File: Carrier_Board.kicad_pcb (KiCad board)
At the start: 4 copper layers, 185.3 x 105.1 mm, 266 parts, among them J18 USB_C_Receptacle_USB2.0_16P, J4 USB3_A_Stacked, J78 Conn_01x03_Pin, J80 Barrel_Jack_Switch, J81 Conn_01x04_Pin, J82 Conn_01x03_Pin, J83 Conn_01x04_Pin, J84 Conn_01x03_Pin, J85 Conn_01x03_Pin, J86 Conn_01x04_Pin, J87 Conn_01x04_Pin, J88 Conn_01x03_Pin, J89 Bus_PCI_Express_x4, J90 RJ45_RB1-125B8G1A, J91 USB3_A_Stacked, J92 USB_A_Stacked, J93 HDMI_A, J94 Bus_M.2_Socket_M, J95 Bus_M.2_Socket_E, M1 Fan_4pin, M2 Fan_4pin, Q78 2N7002, Q79 2N7002, Q80 AON7262E, Q81 2N7002, Q82 2N7002, Q83 2SK3018, Q84 2SK3018, Q85 2SK3018, SW78 SW_Push, SW79 SW_Push, U14 CH224K, U79 TL431DBZ, U80 LM2734X, U81 LM2734X, U82 D3V3XA4B10LP, U83 D3V3XA4B10LP, U84 D3V3XA4B10LP, U85 D3V3XA4B10LP, U86 RTL8111H-CG-RH, U87 D3V3XA4B10LP, U88 D3V3XA4B10LP, U89 D3V3XA4B10LP, U90 D3V3XA4B10LP, U91 D3V3XA4B10LP, U92 D3V3XA4B10LP, U93 D3V3XA4B10LP, Y78 25MHz

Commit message: Started on physical placement of components but footprint got H6 is incoorect. Schematic needs annotation before importing the changes.
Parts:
- moved BT78 420.7 mm to (51.6, 125.4), turned to 90 degrees
- moved H81 414.5 mm to (44.9, 155.2)
- moved H80 399.6 mm to (44.6, 54.4)
- moved J90 336.7 mm to (61.0, 68.5), turned to -90 degrees
- moved H5 305.9 mm to (167.2, 53.7)
- moved J18 288.9 mm to (225.3, 83.0), turned to 90 degrees
- moved H79 252.8 mm to (226.0, 154.9)
- moved SW78 247.4 mm to (171.8, 155.5)
- moved J95 241.9 mm to (93.9, 92.3), turned to -90 degrees
- moved SW79 234.0 mm to (183.6, 155.5)
- moved A78 224.7 mm to (135.3, 110.6), turned to 180 degrees
- moved H78 221.0 mm to (225.7, 54.7)
- moved J93 219.2 mm to (151.8, 150.8), turned to -90 degrees
- moved J4 203.2 mm to (334.4, 158.2)
- moved J91 202.6 mm to (105.4, 147.3)
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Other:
- board size 185.3 x 105.1 mm -> 190 x 110 mm

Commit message: Updating the pcb and recovering placement of components that were reset
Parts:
- removed C100, C109, C110, C113, C115, C130, C148, C99: 100nF/50V, A_HDJ_Library:C_0402_1005Metric
- removed C101, C102, C103, C104, C105, C106, C107, C108: 220nF/50v, A_HDJ_Library:C_0402_1005Metric
- removed C111, C112: 100uF/100v, A_HDJ_Library:CP_Elec_6.3x7.7
- removed C114: 10uF/10V, A_HDJ_Library:C_0402_1005Metric
- removed C116: 560uF/25V, A_HDJ_Library:CP_Elec_6.3x7.7
- removed C117, C118, C119, C120, C121, C122, C128, C152, C154: 100nF/50v, A_HDJ_Library:C_0402_1005Metric
- removed C127, C129, C151, C153: 10uF/50v, A_HDJ_Library:C_0402_1005Metric
- removed C132: 12pF/50V, A_HDJ_Library:C_0402_1005Metric
- removed C133, C134, C135, C136, C140, C141, C142, C143, C144, C145, C146, C147: 100NF/50V, A_HDJ_Library:C_0402_1005Metric
- removed C137, C138, C139: 22mF/10V, A_HDJ_Library:C_0603_1608Metric
- removed C149, C150: 220nF/50V, A_HDJ_Library:C_0402_1005Metric
- removed C155, C156: 220NF/50V, A_HDJ_Library:C_0402_1005Metric
- removed C157, C159: 10uF/10v, A_HDJ_Library:C_0402_1005Metric
- removed C158, C160: 100uF/10v, A_HDJ_Library:C_0402_1005Metric
- removed C86: 1uF/16V, A_HDJ_Library:C_0402_1005Metric
- removed C87, C88: 100uF/50V, A_HDJ_Library:C_0603_1608Metric
- removed C89, C90, C91, C92, C93, C94, C95, C96, C97, C98: 22uF/10V, A_HDJ_Library:C_0603_1608Metric
- removed D100, D101, D102: ESD5V0B03, A_HDJ_Library:D_0402_1005Metric
- removed D103, D94, D95: 1N5819WS, A_HDJ_Library:D_SOD-323
- removed D104: LED, digikey-footprints:LED_0603
- removed D78, D79, D89, D93, D96, D97, D98, D99: ESD9B5.0ST5G, A_HDJ_Library:D_0402_1005Metric
- removed D80, D81, D82: D_Zener, A_HDJ_Library:D_0402_1005Metric
- removed D83, D84, D85, D86, D87, D88: D_Schottky, A_HDJ_Library:D_SMA
- removed D90, D91: LED, A_HDJ_Library:LED_0603_1608Metric
- removed D92: +3V3 Izt=5mA, Diode_SMD:D_SOD-323
- removed F78, F79, F80, F81: 6V/1A, A_HDJ_Library:Fuse_0805_2012Metric
- removed F82: 6V/50MA, A_HDJ_Library:C_0603_1608Metric
- removed H82, H83: MountingHole_M2.0, A_HDJ_Library:MountingHole_3.2mm_M3_Pad_Via
- removed J80: Barrel_Jack_Switch, A_HDJ_Library:DC_Jack_DC007B_30V_10A
- removed J81, J83, J86, J87: Conn_01x04_Pin, A_HDJ_Library:PinHeader_1x04_P2.54mm_Vertical
- removed J82, J84, J85, J88: Conn_01x03_Pin, A_HDJ_Library:PinHeader_1x03_P2.54mm_Vertical
- removed J89: Bus_PCI_Express_x4, A_HDJ_Library:PCIe_x4_Gen3Slot_Connectors
- removed J90: RJ45_RB1-125B8G1A, A_HDJ_Library:RJ45_UDE_RB1-125B8G1A
- removed JP78: Jumper_3_Bridged12, A_HDJ_Library:PinHeader_1x03_P2.54mm_Vertical
- removed JP79: SolderJumper_2_Open, Jumper:SolderJumper-2_P1.3mm_Bridged_RoundedPad1.0x1.5mm
- removed L78, L79: 2.2UH/4.3A, A_HDJ_Library:L_Sunlord_SWPA4020S
- removed Q78, Q81, Q82: 2N7002, A_HDJ_Library:SOT-23
- removed Q79: 2N7002, Package_TO_SOT_SMD:SOT-23
- removed Q80: AON7262E, A_HDJ_Library:MOSFET_PDFN8_3.3x3.3
- removed Q83, Q84: 2SK3018, A_HDJ_Library:SOT-23
- removed R100, R86, R91, R93: 100K/1%, A_HDJ_Library:R_0402_1005Metric
- removed R101, R99: 2.2k/1%, A_HDJ_Library:R_0402_1005Metric
- removed R102, R98: 100k/1%, A_HDJ_Library:R_0402_1005Metric
- removed R103, R94: 100R/1%, A_HDJ_Library:R_0402_1005Metric
- removed R104, R108, R109, R84, R95, R97: 10k/1%, A_HDJ_Library:R_0402_1005Metric
- removed R105, R112, R113, R114, R116: 21.5k/1%, A_HDJ_Library:R_0402_1005Metric
- removed R106, R110, R111, R118, R120, R121: 4.7k/1%, A_HDJ_Library:R_0402_1005Metric
- removed R107: 75k/1%, A_HDJ_Library:R_0402_1005Metric
- removed R115, R117: 100/1%, A_HDJ_Library:R_0402_1005Metric
- removed R119: 0/1%, Resistor_SMD:R_0201_0603Metric
- removed R122: 10\K/1%, A_HDJ_Library:R_0603_1608Metric
- removed R123: 10k/1%, A_HDJ_Library:R_0603_1608Metric
- removed R124: 2.49K/1%, A_HDJ_Library:R_0603_1608Metric
- removed R125, R133: 1M/1%, A_HDJ_Library:R_0402_1005Metric
- removed R126, R127, R129, R130, R135, R136, R137, R138, R139, R140, R141, R142: 470R/1%, A_HDJ_Library:R_0402_1005Metric
- removed R128: 1M, A_HDJ_Library:R_0402_1005Metric
- removed R131: 1K/1%, A_HDJ_Library:R_0402_1005Metric
- removed R144, R146, R147, R148: 0R/1%, A_HDJ_Library:R_0402_1005Metric
- removed R145, R87: 2.2K/1%, A_HDJ_Library:R_0402_1005Metric
- removed R149, R150, R88: 10K/1%, A_HDJ_Library:R_0402_1005Metric
- removed R85, R96: 1k/1%, A_HDJ_Library:R_0402_1005Metric
- removed R89: 56K/1%, A_HDJ_Library:R_0402_1005Metric
- removed SW78, SW79: SW_Push, A_HDJ_Library:SW_Push_6x6x6
- removed TH78: Thermistor_NTC, A_HDJ_Library:R_0603_1608Metric
- removed TP79, TP80, TP82, TP83, TP84, TP85, TP86, TP87, TP89, TP90: TestPoint, A_HDJ_Library:TestPoint_Pad_D1.5mm
- removed U79: TL431DBZ, A_HDJ_Library:SOT-23
- removed U80, U81: LM2734X, Package_TO_SOT_SMD:TSOT-23
- removed U82, U83, U84, U85, U89, U90, U91, U92, U93: D3V3XA4B10LP, A_HDJ_Library:Diodes_UDFN-10_1.0x2.5mm_P0.5mm
- removed U86: RTL8111H-CG-RH, A_HDJ_Library:QFN-32-1EP_4x4mm_P0.4mm_EP2.65x2.65mm
- removed U87, U88: D3V3XA4B10LP, Package_DFN_QFN:Diodes_UDFN-10_1x2.5mm_P0.5mm
- removed Y78: 25MHz, A_HDJ_Library:Crystal_SMD_3225-4Pin_3.2x2.5mm
- added C1: 220nF/50v, A_HDJ_Library:C_0402_1005Metric, F.Cu at (476.1, -68.2)
- added C10: 100nF/50V, A_HDJ_Library:C_0402_1005Metric, F.Cu at (478.9, -60.3)
- added C11: 100uF/100v, A_HDJ_Library:CP_Elec_6.3x7.7, F.Cu at (469.4, -65.1)
- added C12: 100uF/100v, A_HDJ_Library:CP_Elec_6.3x7.7, F.Cu at (469.4, -56.9)
- added C13: 100nF/50V, A_HDJ_Library:C_0402_1005Metric, F.Cu at (481.8, -68.2)
- added C14: 10uF/10V, A_HDJ_Library:C_0402_1005Metric, F.Cu at (481.8, -66.2)
- added C15: 100nF/50V, A_HDJ_Library:C_0402_1005Metric, F.Cu at (481.8, -64.2)
- added C16: 560uF/25V, A_HDJ_Library:CP_Elec_6.3x7.7, F.Cu at (469.4, -48.8)
- added C17: 100NF/50V, A_HDJ_Library:C_0402_1005Metric, F.Cu at (504.2, 1.94)
- added C18: 100NF/50V, A_HDJ_Library:C_0402_1005Metric, F.Cu at (504.2, 3.90)
- added C19: 100NF/50V, A_HDJ_Library:C_0402_1005Metric, F.Cu at (504.2, 5.88)
- added C2: 220nF/50v, A_HDJ_Library:C_0402_1005Metric, F.Cu at (476.1, -66.2)
- added C20: 100NF/50V, A_HDJ_Library:C_0402_1005Metric, F.Cu at (507.0, 1.94)
- added C21: 100NF/50V, A_HDJ_Library:C_0402_1005Metric, F.Cu at (507.0, 3.90)
- added C22: 100NF/50V, A_HDJ_Library:C_0402_1005Metric, F.Cu at (507.0, 5.88)
- added C23: 100NF/50V, A_HDJ_Library:C_0402_1005Metric, F.Cu at (509.9, 1.94)
- added C24: 100NF/50V, A_HDJ_Library:C_0402_1005Metric, F.Cu at (509.9, 3.90)
- added C25: 100nF/50V, A_HDJ_Library:C_0402_1005Metric, F.Cu at (509.9, 5.88)
- added C26: 100NF/50V, A_HDJ_Library:C_0402_1005Metric, F.Cu at (501.3, -21.4)
- added C27: 100NF/50V, A_HDJ_Library:C_0402_1005Metric, F.Cu at (501.3, -19.4)
- added C28: 100NF/50V, A_HDJ_Library:C_0402_1005Metric, F.Cu at (501.3, -17.4)
- added C29: 100NF/50V, A_HDJ_Library:C_0402_1005Metric, F.Cu at (501.3, -15.5)
- added C3: 220nF/50v, A_HDJ_Library:C_0402_1005Metric, F.Cu at (476.1, -64.2)
- added C30: 22mF/10V, A_HDJ_Library:C_0603_1608Metric, F.Cu at (504.7, -21.1)
- added C31: 22mF/10V, A_HDJ_Library:C_0603_1608Metric, F.Cu at (504.7, -18.6)
- added C32: 22mF/10V, A_HDJ_Library:C_0603_1608Metric, F.Cu at (504.7, -16.1)
- added C33: 100nF/50v, A_HDJ_Library:C_0402_1005Metric, F.Cu at (480.6, -40.1)
- added C34: 100nF/50v, A_HDJ_Library:C_0402_1005Metric, F.Cu at (480.6, -38.1)
- added C35: 100nF/50v, A_HDJ_Library:C_0402_1005Metric, F.Cu at (480.6, -36.1)
- added C36: 100nF/50v, A_HDJ_Library:C_0402_1005Metric, F.Cu at (480.6, -34.2)
- added C37: 100nF/50v, A_HDJ_Library:C_0402_1005Metric, F.Cu at (480.6, -32.2)
- added C4: 220nF/50v, A_HDJ_Library:C_0402_1005Metric, F.Cu at (476.1, -62.3)
- added C40: 100nF/50v, A_HDJ_Library:C_0402_1005Metric, F.Cu at (480.6, -30.2)
- added C41: 100nF/50v, A_HDJ_Library:C_0402_1005Metric, F.Cu at (483.5, -40.1)
- added C44: 10uF/50v, A_HDJ_Library:C_0402_1005Metric, F.Cu at (483.5, -38.1)
- added C45: 10uF/50v, A_HDJ_Library:C_0402_1005Metric, F.Cu at (483.5, -36.1)
- added C46: 100nF/50V, A_HDJ_Library:C_0402_1005Metric, F.Cu at (483.5, -34.2)
- added C47: 12pF/50V, A_HDJ_Library:C_0402_1005Metric, F.Cu at (483.5, -32.2)
- added C49: 220nF/50V, A_HDJ_Library:C_0402_1005Metric, F.Cu at (433.4, -15.1)
- added C5: 220nF/50v, A_HDJ_Library:C_0402_1005Metric, F.Cu at (476.1, -60.3)
- added C50: 220nF/50V, A_HDJ_Library:C_0402_1005Metric, F.Cu at (433.4, -13.1)
- added C51: 10uF/50v, A_HDJ_Library:C_0402_1005Metric, F.Cu at (433.4, -11.2)
- added C52: 100nF/50v, A_HDJ_Library:C_0402_1005Metric, F.Cu at (433.4, -9.21)
- added C53: 10uF/50v, A_HDJ_Library:C_0402_1005Metric, F.Cu at (436.3, -15.1)
- added C54: 100nF/50v, A_HDJ_Library:C_0402_1005Metric, F.Cu at (436.3, -13.1)
- added C55: 220NF/50V, A_HDJ_Library:C_0402_1005Metric, F.Cu at (436.3, -11.2)
- added C56: 220NF/50V, A_HDJ_Library:C_0402_1005Metric, F.Cu at (436.3, -9.21)
- added C57: 10uF/10v, A_HDJ_Library:C_0402_1005Metric, F.Cu at (439.1, -15.1)
- added C58: 100uF/10v, A_HDJ_Library:C_0402_1005Metric, F.Cu at (439.1, -13.1)
- added C59: 10uF/10v, A_HDJ_Library:C_0402_1005Metric, F.Cu at (439.1, -11.2)
- added C6: 220nF/50v, A_HDJ_Library:C_0402_1005Metric, F.Cu at (478.9, -68.2)
- added C60: 100uF/10v, A_HDJ_Library:C_0402_1005Metric, F.Cu at (439.1, -9.21)
- added C61: 1uF/16V, A_HDJ_Library:C_0402_1005Metric, F.Cu at (452.1, -53.9)
- added C62: 1uF/16V, A_HDJ_Library:C_0402_1005Metric, F.Cu at (452.1, -52.0)
- added C63: 1uF/16V, A_HDJ_Library:C_0402_1005Metric, F.Cu at (452.1, -50.0)
- added C64: 22uF/10V, A_HDJ_Library:C_0603_1608Metric, F.Cu at (439.0, -65.6)
- added C65: 22uF/10V, A_HDJ_Library:C_0603_1608Metric, F.Cu at (439.0, -63.1)
- added C66: 1uF/16V, A_HDJ_Library:C_0402_1005Metric, F.Cu at (452.1, -48.0)
- added C67: 22uF/10V, A_HDJ_Library:C_0603_1608Metric, F.Cu at (439.0, -60.6)
- added C68: 22uF/10V, A_HDJ_Library:C_0603_1608Metric, F.Cu at (439.0, -58.1)
- added C69: 1uF/16V, A_HDJ_Library:C_0402_1005Metric, F.Cu at (452.1, -46.0)
- added C7: 220nF/50v, A_HDJ_Library:C_0402_1005Metric, F.Cu at (478.9, -66.2)
- added C70: 100uF/50V, A_HDJ_Library:C_0603_1608Metric, F.Cu at (439.0, -55.6)
- added C71: 100uF/50V, A_HDJ_Library:C_0603_1608Metric, F.Cu at (443.0, -65.6)
- added C74: 22uF/10V, A_HDJ_Library:C_0603_1608Metric, F.Cu at (443.0, -63.1)
- added C75: 22uF/10V, A_HDJ_Library:C_0603_1608Metric, F.Cu at (443.0, -60.6)
- added C76: 22uF/10V, A_HDJ_Library:C_0603_1608Metric, F.Cu at (443.0, -58.1)
- added C77: 22uF/10V, A_HDJ_Library:C_0603_1608Metric, F.Cu at (443.0, -55.6)
- added C8: 220nF/50v, A_HDJ_Library:C_0402_1005Metric, F.Cu at (478.9, -64.2)
- added C9: 100nF/50V, A_HDJ_Library:C_0402_1005Metric, F.Cu at (478.9, -62.3)
- added D1: ESD5V0B03, A_HDJ_Library:D_0402_1005Metric, F.Cu at (489.5, 6.64)
- added D10: ESD9B5.0ST5G, A_HDJ_Library:D_0402_1005Metric, F.Cu at (446.5, -65.9)
- added D11: ESD9B5.0ST5G, A_HDJ_Library:D_0402_1005Metric, F.Cu at (446.5, -63.9)
- added D12: D_Zener, A_HDJ_Library:D_0402_1005Metric, F.Cu at (446.5, -61.9)
- added D13: D_Zener, A_HDJ_Library:D_0402_1005Metric, F.Cu at (446.5, -59.9)
- added D14: D_Zener, A_HDJ_Library:D_0402_1005Metric, F.Cu at (446.5, -57.9)
- added D15: D_Schottky, A_HDJ_Library:D_SMA, F.Cu at (428.1, -78.9)
- added D16: D_Schottky, A_HDJ_Library:D_SMA, F.Cu at (428.1, -74.4)
- added D17: D_Schottky, A_HDJ_Library:D_SMA, F.Cu at (428.1, -69.8)
- added D18: D_Schottky, A_HDJ_Library:D_SMA, F.Cu at (428.1, -65.3)
- added D19: D_Schottky, A_HDJ_Library:D_SMA, F.Cu at (428.1, -60.7)
- added D2: ESD5V0B03, A_HDJ_Library:D_0402_1005Metric, F.Cu at (489.5, 8.63)
- added D20: D_Schottky, A_HDJ_Library:D_SMA, F.Cu at (428.1, -56.2)
- added D21: ESD9B5.0ST5G, A_HDJ_Library:D_0402_1005Metric, F.Cu at (446.5, -55.9)
- added D22: LED, A_HDJ_Library:LED_0603_1608Metric, F.Cu at (434.1, -52.2)
- added D23: LED, A_HDJ_Library:LED_0603_1608Metric, F.Cu at (434.1, -49.6)
- added D24: +3V3 Izt=5mA, Diode_SMD:D_SOD-323, F.Cu at (434.3, -46.8)
- added D25: ESD9B5.0ST5G, A_HDJ_Library:D_0402_1005Metric, F.Cu at (449.4, -65.9)
- added D26: 1N5819WS, A_HDJ_Library:D_SOD-323, F.Cu at (434.9, -4.75)
- added D27: 1N5819WS, A_HDJ_Library:D_SOD-323, F.Cu at (434.9, -1.79)
- added D3: ESD5V0B03, A_HDJ_Library:D_0402_1005Metric, F.Cu at (489.5, 10.6)
- added D4: 1N5819WS, A_HDJ_Library:D_SOD-323, F.Cu at (509.8, -10.9)
- added D5: ESD9B5.0ST5G, A_HDJ_Library:D_0402_1005Metric, F.Cu at (498.4, -21.4)
- added D6: ESD9B5.0ST5G, A_HDJ_Library:D_0402_1005Metric, F.Cu at (498.4, -19.4)
- added D7: ESD9B5.0ST5G, A_HDJ_Library:D_0402_1005Metric, F.Cu at (498.4, -17.4)
- added D8: ESD9B5.0ST5G, A_HDJ_Library:D_0402_1005Metric, F.Cu at (498.4, -15.4)
- added D9: LED, digikey-footprints:LED_0603, F.Cu at (446.0, -14.9)
- added F1: 6V/50MA, A_HDJ_Library:C_0603_1608Metric, F.Cu at (509.6, -8.20)
- added F2: 6V/1A, A_HDJ_Library:Fuse_0805_2012Metric, F.Cu at (510.1, -39.6)
- added F3: 6V/1A, A_HDJ_Library:Fuse_0805_2012Metric, F.Cu at (510.1, -36.6)
- added F4: 6V/1A, A_HDJ_Library:Fuse_0805_2012Metric, F.Cu at (510.1, -33.7)
- added F5: 6V/1A, A_HDJ_Library:Fuse_0805_2012Metric, F.Cu at (510.1, -30.7)
- added H7: MountingHole_M2.0, A_HDJ_Library:MountingHole_3.2mm_M3_Pad_Via, F.Cu at (428.0, -37.1)
- added H8: MountingHole_M2.0, A_HDJ_Library:MountingHole_3.2mm_M3_Pad_Via, F.Cu at (428.0, -29.1)
- added J10: Conn_01x03_Pin, A_HDJ_Library:PinHeader_1x03_P2.54mm_Vertical, F.Cu at (466.0, -8.45)
- added J11: Conn_01x03_Pin, A_HDJ_Library:PinHeader_1x03_P2.54mm_Vertical, F.Cu at (470.7, -8.45)
- added J12: Conn_01x04_Pin, A_HDJ_Library:PinHeader_1x04_P2.54mm_Vertical, F.Cu at (470.7, 1.25)
- added J13: Conn_01x04_Pin, A_HDJ_Library:PinHeader_1x04_P2.54mm_Vertical, F.Cu at (475.3, 1.25)
- added J14: Conn_01x03_Pin, A_HDJ_Library:PinHeader_1x03_P2.54mm_Vertical, F.Cu at (475.3, -8.45)
- added J15: Bus_M.2_Socket_M, A_HDJ_Library:PCIe_M.2_Connectors_P=0.5mm_H=4.2mm_KeyM, F.Cu at (444.5, -34.9)
- added J16: Bus_M.2_Socket_E, A_HDJ_Library:PCIe_M.2_Connectors_P=0.5mm_H=4.2mm_KeyE, F.Cu at (435.2, -26.2)
- added J17: Barrel_Jack_Switch, A_HDJ_Library:DC_Jack_DC007B_30V_10A, F.Cu at (229.4, 70.8)
- added J2: Bus_PCI_Express_x4, A_HDJ_Library:PCIe_x4_Gen3Slot_Connectors, F.Cu at (301.6, 198.6)
- added J3: HDMI_A, A_HDJ_Library:HDMI_A_Molex_208658-1001_Horizontal, F.Cu at (493.7, -3.38)
- added J5: USB_A_Stacked, A_HDJ_Library:USB_A_CUI_UJ2-ADH-TH_Horizontal_Stacked, F.Cu at (502.1, -35.2)
- added J6: RJ45_RB1-125B8G1A, A_HDJ_Library:RJ45_UDE_RB1-125B8G1A, F.Cu at (463.4, -38.0)
- added J7: Conn_01x04_Pin, A_HDJ_Library:PinHeader_1x04_P2.54mm_Vertical, F.Cu at (461.4, 1.25)
- added J8: Conn_01x03_Pin, A_HDJ_Library:PinHeader_1x03_P2.54mm_Vertical, F.Cu at (461.4, -8.45)
- added J9: Conn_01x04_Pin, A_HDJ_Library:PinHeader_1x04_P2.54mm_Vertical, F.Cu at (466.0, 1.25)
- added JP1: Jumper_3_Bridged12, A_HDJ_Library:PinHeader_1x03_P2.54mm_Vertical, F.Cu at (455.8, -52.6)
- added JP2: SolderJumper_2_Open, Jumper:SolderJumper-2_P1.3mm_Bridged_RoundedPad1.0x1.5mm, F.Cu at (426.2, 3.52)
- added L1: 2.2UH/4.3A, A_HDJ_Library:L_Sunlord_SWPA4020S, F.Cu at (447.8, -52.1)
- added L2: 2.2UH/4.3A, A_HDJ_Library:L_Sunlord_SWPA4020S, F.Cu at (447.8, -46.5)
- added Q1: 2N7002, A_HDJ_Library:SOT-23, F.Cu at (505.2, -10.2)
- added Q2: 2SK3018, A_HDJ_Library:SOT-23, F.Cu at (505.2, -5.72)
- added Q3: 2SK3018, A_HDJ_Library:SOT-23, F.Cu at (505.2, -1.27)
- added Q5: 2N7002, A_HDJ_Library:SOT-23, F.Cu at (434.5, -64.6)
- added Q6: 2N7002, Package_TO_SOT_SMD:SOT-23, F.Cu at (426.5, -45.3)
- added Q7: AON7262E, A_HDJ_Library:MOSFET_PDFN8_3.3x3.3, F.Cu at (427.2, -50.7)
- added Q8: 2N7002, A_HDJ_Library:SOT-23, F.Cu at (434.5, -60.2)
- added R10: 470R/1%, A_HDJ_Library:R_0402_1005Metric, F.Cu at (495.3, 10.6)
- added R11: 1M/1%, A_HDJ_Library:R_0402_1005Metric, F.Cu at (495.3, 12.6)
- added R13: 470R/1%, A_HDJ_Library:R_0402_1005Metric, F.Cu at (498.3, 6.64)
- added R14: 470R/1%, A_HDJ_Library:R_0402_1005Metric, F.Cu at (498.3, 8.63)
- added R16: 470R/1%, A_HDJ_Library:R_0402_1005Metric, F.Cu at (498.3, 10.6)
- added R17: 470R/1%, A_HDJ_Library:R_0402_1005Metric, F.Cu at (498.3, 12.6)
- added R20: 10\K/1%, A_HDJ_Library:R_0603_1608Metric, F.Cu at (481.2, -28.0)
- added R206: 21.5k/1%, A_HDJ_Library:R_0402_1005Metric, F.Cu at (431.3, 0.74)
- added R21: 10k/1%, A_HDJ_Library:R_0603_1608Metric, F.Cu at (481.2, -25.5)
- added R22: 2.49K/1%, A_HDJ_Library:R_0603_1608Metric, F.Cu at (481.2, -23.0)
- added R23: 1M/1%, A_HDJ_Library:R_0402_1005Metric, F.Cu at (484.6, -28.2)
- added R24: 470R/1%, A_HDJ_Library:R_0402_1005Metric, F.Cu at (484.6, -26.2)
- added R25: 470R/1%, A_HDJ_Library:R_0402_1005Metric, F.Cu at (484.6, -24.3)
- added R27: 0R/1%, A_HDJ_Library:R_0402_1005Metric, F.Cu at (425.5, -24.2)
- added R28: 2.2K/1%, A_HDJ_Library:R_0402_1005Metric, F.Cu at (425.5, -22.2)
- added R29: 0R/1%, A_HDJ_Library:R_0402_1005Metric, F.Cu at (425.5, -20.2)
- added R3: 470R/1%, A_HDJ_Library:R_0402_1005Metric, F.Cu at (489.5, 12.6)
- added R32: 0R/1%, A_HDJ_Library:R_0402_1005Metric, F.Cu at (425.5, -18.2)
- added R33: 0R/1%, A_HDJ_Library:R_0402_1005Metric, F.Cu at (425.5, -16.2)
- added R34: 10K/1%, A_HDJ_Library:R_0402_1005Metric, F.Cu at (425.5, -14.2)
- added R35: 10K/1%, A_HDJ_Library:R_0402_1005Metric, F.Cu at (425.5, -12.2)
- added R36: 10k/1%, A_HDJ_Library:R_0402_1005Metric, F.Cu at (449.4, -63.9)
- added R37: 1k/1%, A_HDJ_Library:R_0402_1005Metric, F.Cu at (449.4, -61.9)
- added R38: 100K/1%, A_HDJ_Library:R_0402_1005Metric, F.Cu at (449.4, -59.9)
- added R39: 2.2K/1%, A_HDJ_Library:R_0402_1005Metric, F.Cu at (449.4, -57.9)
- added R4: 1M/1%, A_HDJ_Library:R_0402_1005Metric, F.Cu at (492.4, 6.64)
- added R41: 10K/1%, A_HDJ_Library:R_0402_1005Metric, F.Cu at (449.4, -55.9)
- added R43: 56K/1%, A_HDJ_Library:R_0402_1005Metric, F.Cu at (452.3, -65.9)
- added R44: 100K/1%, A_HDJ_Library:R_0402_1005Metric, F.Cu at (452.3, -63.9)
- added R45: 100K/1%, A_HDJ_Library:R_0402_1005Metric, F.Cu at (452.3, -61.9)
- added R46: 100k/1%, A_HDJ_Library:R_0402_1005Metric, F.Cu at (452.3, -59.9)
- added R47: 1k/1%, A_HDJ_Library:R_0402_1005Metric, F.Cu at (452.3, -57.9)
- added R49: 10k/1%, A_HDJ_Library:R_0402_1005Metric, F.Cu at (452.3, -55.9)
- added R5: 470R/1%, A_HDJ_Library:R_0402_1005Metric, F.Cu at (492.4, 8.63)
- added R50: 10k/1%, A_HDJ_Library:R_0402_1005Metric, F.Cu at (455.2, -65.9)
- added R51: 100k/1%, A_HDJ_Library:R_0402_1005Metric, F.Cu at (455.2, -63.9)
- added R52: 2.2k/1%, A_HDJ_Library:R_0402_1005Metric, F.Cu at (455.2, -61.9)
- added R53: 2.2k/1%, A_HDJ_Library:R_0402_1005Metric, F.Cu at (455.2, -59.9)
- added R54: 100K/1%, A_HDJ_Library:R_0402_1005Metric, F.Cu at (455.2, -57.9)
- added R55: 100R/1%, A_HDJ_Library:R_0402_1005Metric, F.Cu at (455.2, -55.9)
- added R56: 10k/1%, A_HDJ_Library:R_0402_1005Metric, F.Cu at (458.1, -65.9)
- added R57: 75k/1%, A_HDJ_Library:R_0402_1005Metric, F.Cu at (458.1, -63.9)
- added R58: 10k/1%, A_HDJ_Library:R_0402_1005Metric, F.Cu at (458.1, -61.9)
- added R59: 21.5k/1%, A_HDJ_Library:R_0402_1005Metric, F.Cu at (458.1, -59.9)
- added R6: 21.5K/1%, A_HDJ_Library:R_0402_1005Metric, F.Cu at (492.4, 10.6)
- added R60: 4.7k/1%, A_HDJ_Library:R_0402_1005Metric, F.Cu at (458.1, -57.9)
- added R63: 10k/1%, A_HDJ_Library:R_0402_1005Metric, F.Cu at (425.5, -5.22)
- added R64: 4.7k/1%, A_HDJ_Library:R_0402_1005Metric, F.Cu at (425.5, -3.23)
- added R65: 4.7k/1%, A_HDJ_Library:R_0402_1005Metric, F.Cu at (425.5, -1.25)
- added R66: 100R/1%, A_HDJ_Library:R_0402_1005Metric, F.Cu at (458.1, -55.9)
- added R67: 21.5k/1%, A_HDJ_Library:R_0402_1005Metric, F.Cu at (425.5, 0.74)
- added R68: 21.5k/1%, A_HDJ_Library:R_0402_1005Metric, F.Cu at (428.4, -5.22)
- added R69: 100/1%, A_HDJ_Library:R_0402_1005Metric, F.Cu at (428.4, -3.23)
- added R7: 470R/1%, A_HDJ_Library:R_0402_1005Metric, F.Cu at (492.4, 12.6)
- added R70: 21.5k/1%, A_HDJ_Library:R_0402_1005Metric, F.Cu at (428.4, -1.25)
- added R71: 100/1%, A_HDJ_Library:R_0402_1005Metric, F.Cu at (428.4, 0.74)
- added R72: 4.7k/1%, A_HDJ_Library:R_0402_1005Metric, F.Cu at (431.3, -5.22)
- added R73: 0/1%, Resistor_SMD:R_0201_0603Metric, F.Cu at (434.0, 4.11)
- added R74: 4.7k/1%, A_HDJ_Library:R_0402_1005Metric, F.Cu at (431.3, -3.23)
- added R75: 4.7k/1%, A_HDJ_Library:R_0402_1005Metric, F.Cu at (431.3, -1.25)
- added R8: 470R/1%, A_HDJ_Library:R_0402_1005Metric, F.Cu at (495.3, 6.64)
- added R9: 470R/1%, A_HDJ_Library:R_0402_1005Metric, F.Cu at (495.3, 8.63)
- added SW1: SW_Push, A_HDJ_Library:SW_Push_6x6x6, F.Cu at (174.1, 150.2)
- added SW2: SW_Push, A_HDJ_Library:SW_Push_6x6x6, F.Cu at (186.0, 150.2)
- added TH1: Thermistor_NTC, A_HDJ_Library:R_0603_1608Metric, F.Cu at (430.4, 3.00)
- added TP1: TestPoint, A_HDJ_Library:TestPoint_Pad_D1.5mm, F.Cu at (476.4, -57.5)
- added TP12: TestPoint, A_HDJ_Library:TestPoint_Pad_D1.5mm, F.Cu at (434.5, 1.46)
- added TP13: TestPoint, A_HDJ_Library:TestPoint_Pad_D1.5mm, F.Cu at (449.4, -72.3)
- added TP2: TestPoint, A_HDJ_Library:TestPoint_Pad_D1.5mm, F.Cu at (442.3, -14.3)
- added TP3: TestPoint, A_HDJ_Library:TestPoint_Pad_D1.5mm, F.Cu at (445.9, -79.4)
- added TP4: TestPoint, A_HDJ_Library:TestPoint_Pad_D1.5mm, F.Cu at (445.9, -75.9)
- added TP5: TestPoint, A_HDJ_Library:TestPoint_Pad_D1.5mm, F.Cu at (445.9, -72.3)
- added TP6: TestPoint, A_HDJ_Library:TestPoint_Pad_D1.5mm, F.Cu at (445.9, -68.8)
- added TP8: TestPoint, A_HDJ_Library:TestPoint_Pad_D1.5mm, F.Cu at (449.4, -79.4)
- added TP9: TestPoint, A_HDJ_Library:TestPoint_Pad_D1.5mm, F.Cu at (449.4, -75.9)
- added U1: D3V3XA4B10LP, A_HDJ_Library:Diodes_UDFN-10_1.0x2.5mm_P0.5mm, F.Cu at (504.2, 8.88)
- added U10: D3V3XA4B10LP, A_HDJ_Library:Diodes_UDFN-10_1.0x2.5mm_P0.5mm, F.Cu at (463.5, 13.2)
- added U11: D3V3XA4B10LP, A_HDJ_Library:Diodes_UDFN-10_1.0x2.5mm_P0.5mm, F.Cu at (466.4, 13.2)
- added U12: D3V3XA4B10LP, A_HDJ_Library:Diodes_UDFN-10_1.0x2.5mm_P0.5mm, F.Cu at (469.4, 13.2)
- added U13: TL431DBZ, A_HDJ_Library:SOT-23, F.Cu at (434.5, -55.7)
- added U15: LM2734X, Package_TO_SOT_SMD:TSOT-23, F.Cu at (439.7, -51.9)
- added U16: LM2734X, Package_TO_SOT_SMD:TSOT-23, F.Cu at (439.7, -47.2)
- added U2: D3V3XA4B10LP, A_HDJ_Library:Diodes_UDFN-10_1.0x2.5mm_P0.5mm, F.Cu at (507.2, 8.88)
- added U3: D3V3XA4B10LP, A_HDJ_Library:Diodes_UDFN-10_1.0x2.5mm_P0.5mm, F.Cu at (489.5, -20.3)
- added U4: D3V3XA4B10LP, A_HDJ_Library:Diodes_UDFN-10_1.0x2.5mm_P0.5mm, F.Cu at (492.5, -20.3)
- added U5: D3V3XA4B10LP, A_HDJ_Library:Diodes_UDFN-10_1.0x2.5mm_P0.5mm, F.Cu at (495.4, -20.3)
- added U6: RTL8111H-CG-RH, A_HDJ_Library:QFN-32-1EP_4x4mm_P0.4mm_EP2.65x2.65mm, F.Cu at (482.3, -18.6)
- added U7: D3V3XA4B10LP, Package_DFN_QFN:Diodes_UDFN-10_1x2.5mm_P0.5mm, F.Cu at (460.5, -15.1)
- added U8: D3V3XA4B10LP, Package_DFN_QFN:Diodes_UDFN-10_1x2.5mm_P0.5mm, F.Cu at (463.5, -15.1)
- added U9: D3V3XA4B10LP, A_HDJ_Library:Diodes_UDFN-10_1.0x2.5mm_P0.5mm, F.Cu at (460.5, 13.2)
- added Y1: 25MHz, A_HDJ_Library:Crystal_SMD_3225-4Pin_3.2x2.5mm, F.Cu at (467.6, -15.0)
- C78, C79, C80, C81: value 1uF/16V -> 22uF/10V; footprint A_HDJ_Library:C_0402_1005Metric -> A_HDJ_Library:C_0603_1608Metric
- C84, C85: value 22uF/10V -> 100nF/50V; footprint A_HDJ_Library:C_0603_1608Metric -> A_HDJ_Library:C_0402_1005Metric
- H6: footprint A_HDJ_Library:MountingHole_3.2mm_M3_Pad_Via -> A_HDJ_Library:MountingHole_3mm_M2_Pad_TopOnly
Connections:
- C78 pad 1: GND -> +5V
- C78 pad 2: Net-(U14-VDD) -> GND
- C79 pad 1: Net-(Q80-S_1) -> +3.3V
- C79 pad 2: +12VA -> GND
- C80 pad 1: Net-(Q78-G) -> +5V
- C81 pad 1: Net-(D89-A2) -> +3.3V
- C82 pad 1: GND -> +5V
- C82 pad 2: VDC -> GND
- C83 pad 1: VDC -> +3.3V
- C84 pad 1: GND -> +5V
- C84 pad 2: VDC -> GND
- C85 pad 1: VDC -> Net-(D27-K)
- J4 pad 1: (no net) -> Net-(J4A-VBUS1)
- J4 pad 2: (no net) -> /USB 2.0 & 3.0/CON_USB3_D_N
- J4 pad 3: (no net) -> /USB 2.0 & 3.0/CON_USB3_D_P
- J4 pad 4: (no net) -> GND
- J4 pad 5: (no net) -> /USB 2.0 & 3.0/CON_USB3_SSRX_N
- J4 pad 6: (no net) -> /USB 2.0 & 3.0/CON_USB3_SSRX_P
- J4 pad 7: (no net) -> GND
- J4 pad 8: (no net) -> /USB 2.0 & 3.0/CON_USB3_SSTX_N
- J4 pad 9: (no net) -> /USB 2.0 & 3.0/CON_USB3_SSTX_P
- M2 pad 2: Net-(D95-K) -> Net-(D27-K)
- R90 pad 1: Net-(Q78-G) -> Net-(Q5-G)
- R92 pad 2: Net-(Q78-G) -> Net-(Q5-G)

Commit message: Footprint of the GPIO connectors mismatch 1x3 mine and reference schem but lecture is 1x4  Physical placement complete
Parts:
- removed J94: Bus_M.2_Socket_M, A_HDJ_Library:PCIe_M.2_Connectors_P=0.5mm_H=4.2mm_KeyM
- removed J95: Bus_M.2_Socket_E, A_HDJ_Library:PCIe_M.2_Connectors_P=0.5mm_H=4.2mm_KeyE
- moved J6 438.2 mm to (42.8, 85.0), turned to 90 degrees
- moved J5 413.3 mm to (148.2, 178.2)
- moved H8 390.1 mm to (60.5, 101.7)
- moved J15 379.4 mm to (90.5, 101.5), turned to -90 degrees
- moved M2 376.6 mm to (128.3, 39.1)
- moved J13 370.6 mm to (108.5, 53.4)
- moved J14 367.8 mm to (112.7, 53.3)
- moved J8 360.6 mm to (108.3, 64.9), turned to 90 degrees
- moved J12 357.7 mm to (116.8, 53.3)
- moved J11 355.1 mm to (121.0, 53.1)
- moved J10 342.9 mm to (131.1, 65.3)
- moved J9 339.7 mm to (130.2, 52.7)
- moved J7 339.0 mm to (126.3, 52.8)
- moved M1 332.4 mm to (173.8, 66.8), turned to 90 degrees
- moved JP1 311.6 mm to (173.8, 79.8)
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
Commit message: Revised missing components in the GPIO Schema and completed the general placement of the pcb components
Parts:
- added J19: Conn_01x04_Pin, A_HDJ_Library:PinHeader_1x04_P2.54mm_Vertical, F.Cu at (70.4, 53.5)
- added J20: Conn_01x04_Pin, A_HDJ_Library:PinHeader_1x04_P2.54mm_Vertical, F.Cu at (64.3, 53.2)
- added J21: Conn_01x04_Pin, A_HDJ_Library:PinHeader_1x04_P2.54mm_Vertical, F.Cu at (56.0, 53.4)
- added U17: D3V3XA4B10LP, Package_DFN_QFN:Diodes_UDFN-10_1x2.5mm_P0.5mm, F.Cu at (45.8, 38.0)
- moved J11 118.5 mm to (54.0, 151.0)
- moved J14 111.6 mm to (58.8, 151.1)
- moved J10 106.8 mm to (67.5, 151.0)
- moved J8 97.3 mm to (63.1, 151.1), turned to 0 degrees
- moved J13 56.6 mm to (51.9, 53.4)
- moved J12 56.5 mm to (60.2, 53.3)
- moved J7 51.7 mm to (74.7, 53.5)
- moved J9 50.9 mm to (79.4, 53.5)
- moved JP1 4.82 mm to (177.2, 76.3)
- moved M1 4.21 mm to (176.8, 69.8)
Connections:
- A78 pad 128: /LattePanda Module/GPP_D0 -> /GPIO/GPP_D0
- A78 pad 130: /LattePanda Module/GPP_D1 -> /GPIO/GPP_D1
- A78 pad 132: /LattePanda Module/GPP_D2 -> /GPIO/GPP_D2
- A78 pad 134: /LattePanda Module/GPP_D3 -> /GPIO/GPP_D3

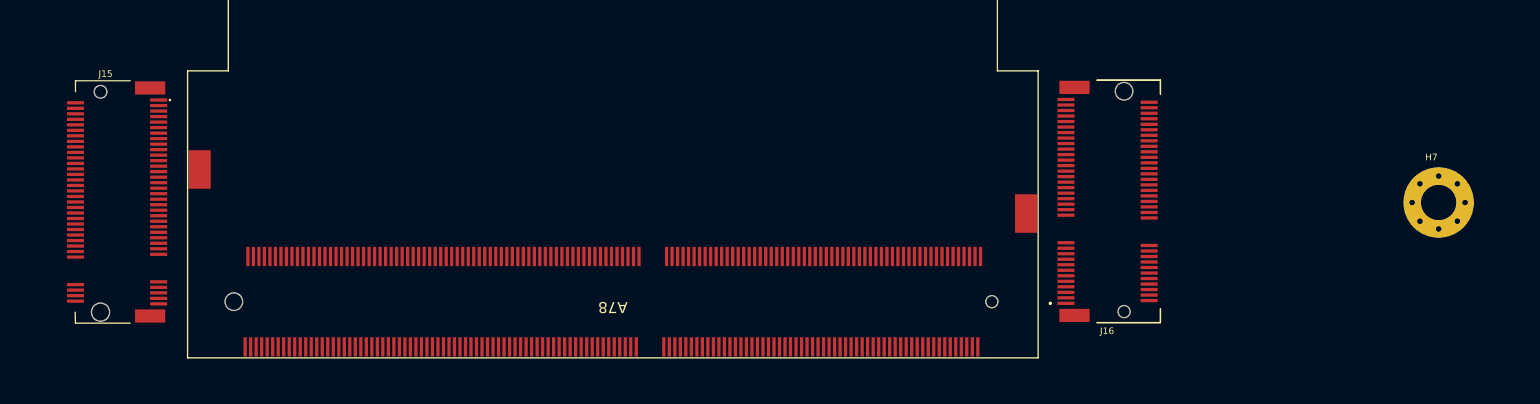
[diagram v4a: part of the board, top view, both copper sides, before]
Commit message: Locked the m.2 mounting holes exactl in place
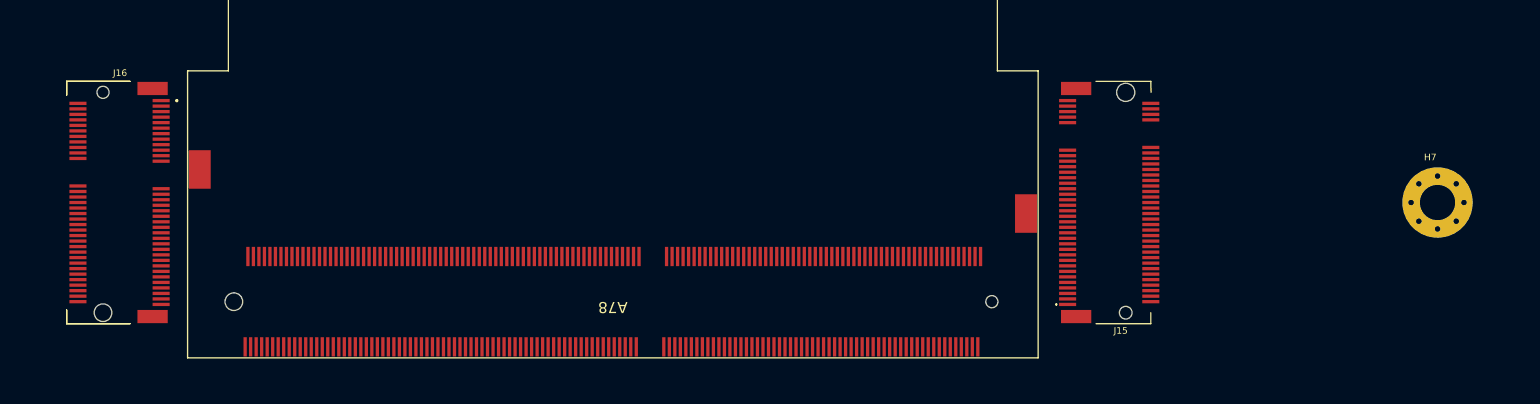
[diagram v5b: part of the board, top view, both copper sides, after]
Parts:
- moved J15 89.7 mm to (180.2, 101.6), turned to 90 degrees
- moved J16 84.2 mm to (94.3, 92.3), turned to -90 degrees
- moved H7 0.10 mm to (210.2, 101.6)

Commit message: First impedence matching successful by using 9 and then increase spacing 1. skew went from .078 to 0 after increase spacing hot key 1 combo
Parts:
- moved C49 363.6 mm to (92.2, 110.5), turned to 180 degrees
- moved C50 362.6 mm to (92.2, 109.4), turned to 180 degrees
- moved C55 353.7 mm to (94.9, 81.3), turned to 180 degrees
- moved H7 154.7 mm to (55.6, 107.5), turned to 180 degrees
- moved C10 137.3 mm to (348.2, -18.4)
- moved C11 137.3 mm to (338.7, -23.2)
- moved C12 137.3 mm to (338.7, -15.1)
- moved C13 137.3 mm to (351.1, -26.3)
- moved C131 137.3 mm to (315.7, 91.2)
- moved C14 137.3 mm to (351.1, -24.3)
- moved C15 137.3 mm to (351.1, -22.4)
- moved C16 137.3 mm to (338.7, -6.90)
- moved C17 137.3 mm to (373.4, 43.8)
- moved C18 137.3 mm to (373.4, 45.8)
- moved C19 137.3 mm to (373.4, 47.8)
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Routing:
- net /LattePanda Module/HSIO_2_TX+: track 0.00 -> 19.0 mm
- net /LattePanda Module/HSIO_2_TX-: track 0.00 -> 19.0 mm
- net /M.2 M Key/CON_PCIE_TX1-: track 0.00 -> 2.72 mm
- net /M.2 M Key/CON_PCIE_TX1+: track 0.00 -> 2.72 mm

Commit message: Finished differential pair routing on J15 moving on to J16 m.2 key
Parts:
- removed J91: USB3_A_Stacked, A_HDJ_Library:USB3_A_Molex_48406-0001_Horizontal_Stacked
- removed J92: USB_A_Stacked, A_HDJ_Library:USB_A_CUI_UJ2-ADH-TH_Horizontal_Stacked
- removed J93: HDMI_A, A_HDJ_Library:HDMI_A_Molex_208658-1001_Horizontal
- moved J3 307.9 mm to (126.7, 149.8), turned to -90 degrees
- moved J4 229.7 mm to (105.0, 146.8)
- moved C56 218.9 mm to (92.3, 82.2), turned to 180 degrees
- moved J2 117.8 mm to (196.6, 145.3), turned to 90 degrees
- moved J5 70.2 mm to (86.1, 145.4), turned to 90 degrees
- moved J6 21.2 mm to (143.4, 138.9)
- moved C55 2.63 mm to (92.3, 81.1)
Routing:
- net /LattePanda Module/REFCLK0+: track 0.00 -> 41.9 mm, vias 0 -> 2
- net /LattePanda Module/REFCLK0-: track 0.00 -> 41.9 mm, vias 0 -> 2
- net /LattePanda Module/HSIO_2_RX+: track 0.00 -> 25.4 mm
- net /LattePanda Module/HSIO_2_RX-: track 0.00 -> 25.4 mm
